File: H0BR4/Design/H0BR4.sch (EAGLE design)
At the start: 26 parts, among them P1 HEXABIT_17.32, U1 STM32G0B1CEU6NUFQFPN48_STM32_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, U2 LSM6DS3TR-C, U3 STMICROELECTRONICS_LSM303AGRT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, X1 CSTNE8M00G550000R0

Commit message: -Improving the layout
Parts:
- U1: value STM32G0B1CEU6NUFQFPN48_STM32_STM -> STM32G0B1CEU6N; device HEXABITZ_ICs:STM32G0B1CEU6NUFQFPN48_STM32_STM -> HEXABITZ_ICs:STM32G0B1CEU6N
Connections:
- net GND: no longer U1.PB3, U1.PB4, U1.PB5

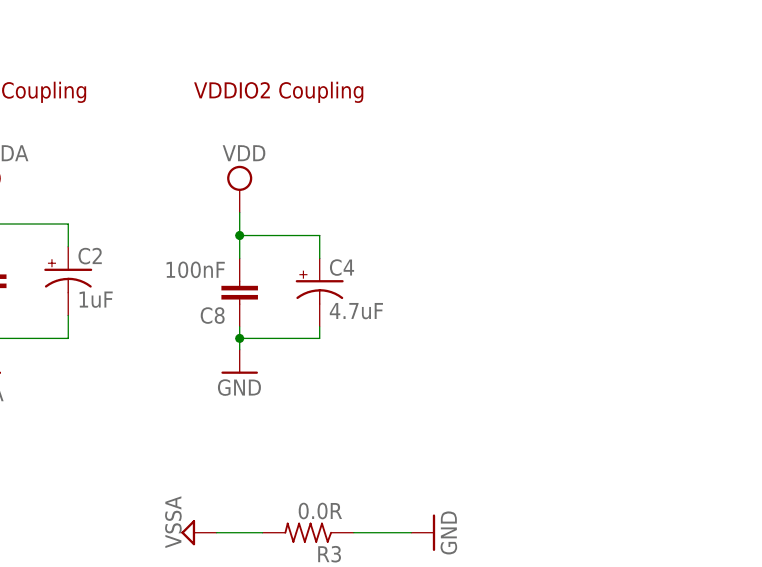
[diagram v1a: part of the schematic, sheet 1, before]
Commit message: update the logo add TVS
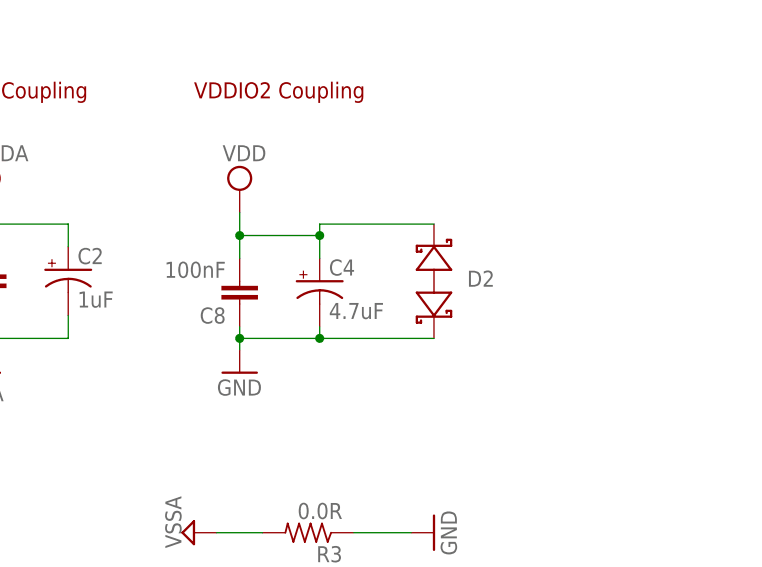
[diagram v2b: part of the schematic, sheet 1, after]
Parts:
- added D2: BOURNS_CDSOD323-T03SCBOURNS_CDSOD323-T03SC_0_0, HEXABITZ_RCLS:BOURNS_CDSOD323-T03SCBOURNS_CDSOD323-T03SC_0_0
- added TRIMBLE-LOGO1: HEXA-LOGO, HEXABITZ_USER_INTERFACE_PARTS:HEXA-LOGO
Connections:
- net GND: now also D2.A
- net VDD: now also D2.C
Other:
- note added: "H0BR4"
- note added: "H0BR4_Backend"
- note added: "H0BR4_Frontend"
- note removed: "H0BR41"
- note removed: "H0BR41_Backend"
- note removed: "H0BR41_Frontend"
- note removed: "Ibrahim Zaeiter"
